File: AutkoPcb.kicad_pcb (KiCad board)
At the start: 2 copper layers, 83.8 x 105.5 mm, 60 parts, among them IC201 TEENSY_4.1, J101 JST 2.56mm, J102 JST 2.56mm, J103 JST 2.56mm, J104 JST 2.56mm, J105 JST 2.56mm, J107 JST 2.56mm, J108 JST 2.56mm, J109 JST 2.56mm, J110 JST 2.56mm, J111 JST 2.56mm, J112 JST 2.56mm, J113 JST 2.56mm, J114 Conn_01x12_Pin, J401 Conn_01x03_Male, J501 Conn_01x03_Male, J601 JST 2.56mm, J701 JST 2.56mm, J801 JST 2.56mm, J901 ARK 5mm, J902 Barrel_Jack_MountingPin, J903 Barrel_Jack_MountingPin, J904 ARK 5mm, J905 JST 2.54mm, J906 JST 2.54mm, J907 JST 2.56mm, SW1001 SW_Push, SW1101 SW_Push, SW1201 SW_Push, SW1301 SW_Push, U901 AZ1117-3.3

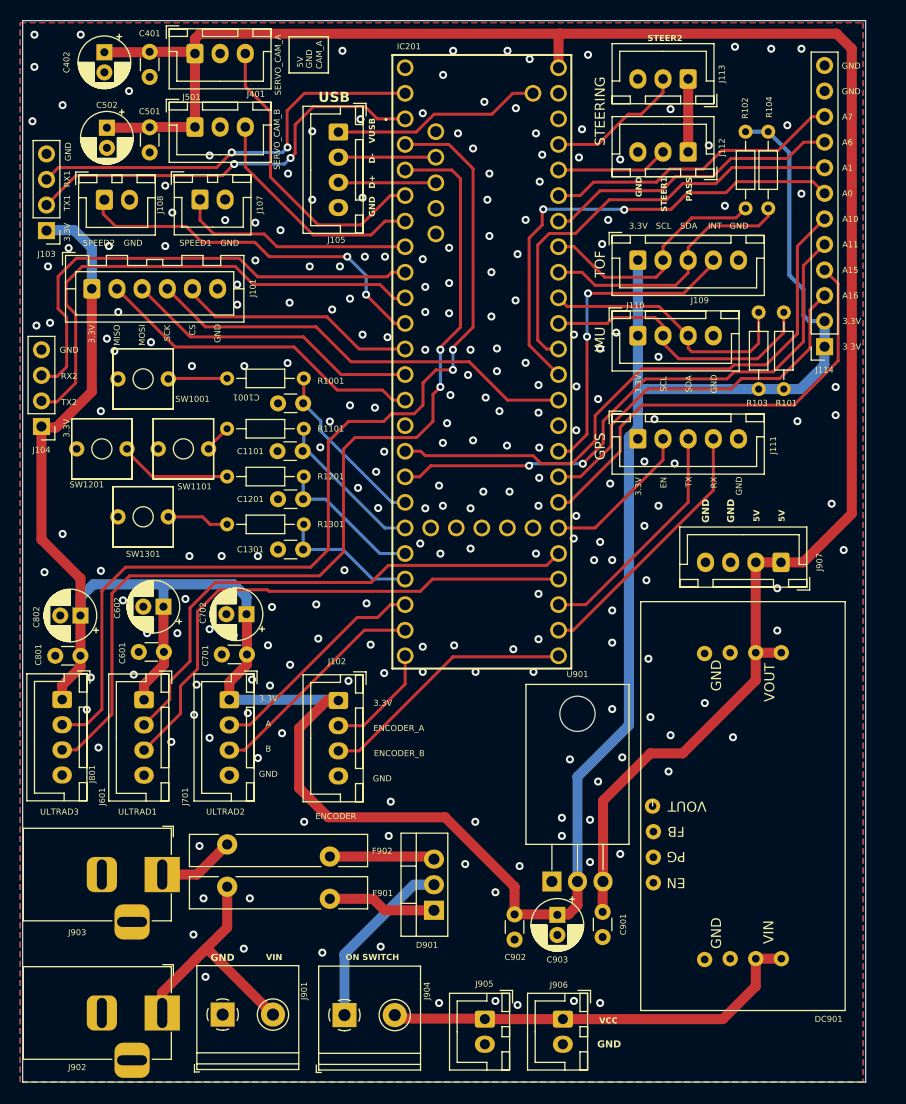
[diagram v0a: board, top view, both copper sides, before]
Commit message: changing labels on PCB
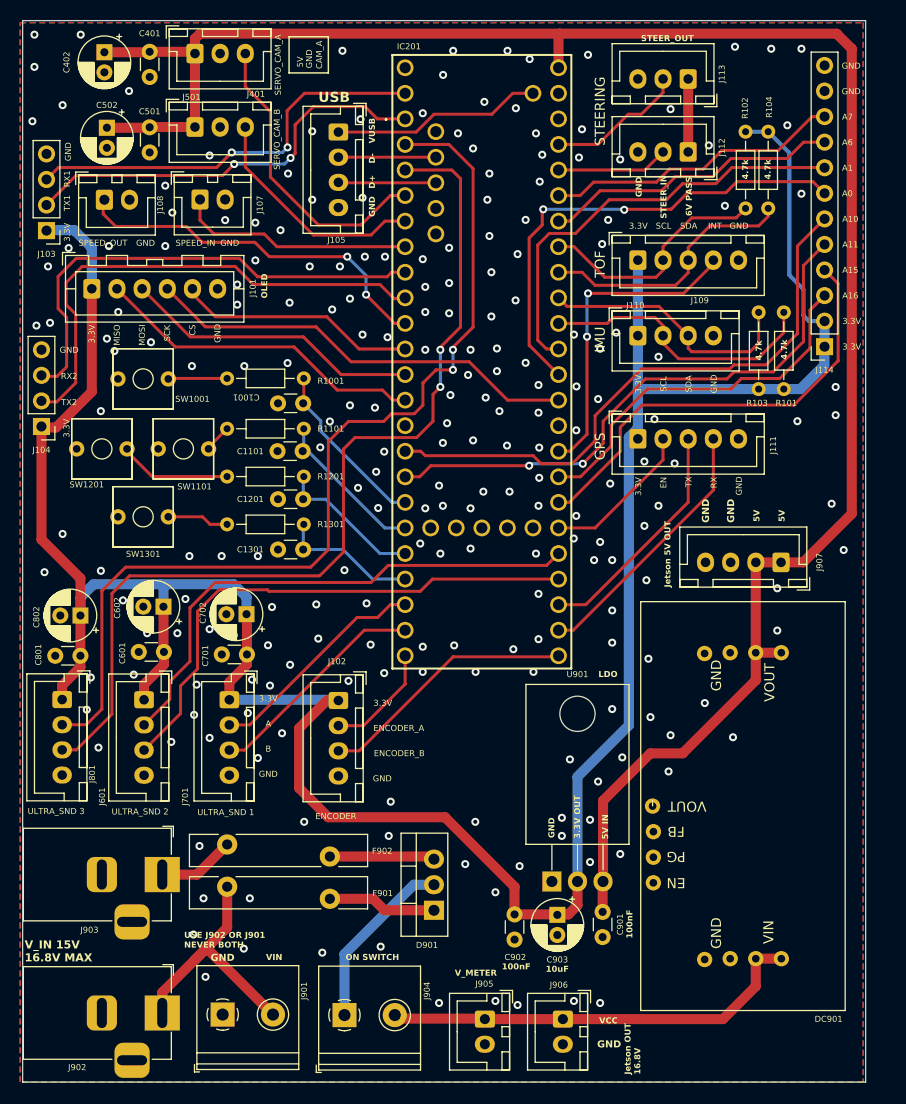
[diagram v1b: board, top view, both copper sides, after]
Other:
- board text added: "100nF"
- board text added: "10uF"
- board text added: "3.3V OUT"
- board text added: "4.7k"
- board text added: "5V IN"
- board text added: "6V PASS"
- board text added: "Jetson 5V OUT"
- board text added: "Jetson OUT 16.8V"
- board text added: "LDO"
- board text added: "OLED"
- board text added: "SPEED_IN"
- board text added: "SPEED_OUT"
- board text added: "STEER_IN"
- board text added: "STEER_OUT"
- board text added: "ULTRA_SND 1"
- board text added: "ULTRA_SND 2"
- board text added: "ULTRA_SND 3"
- board text added: "USE J902 OR J901 NEVER BOTH"
- board text added: "V_IN 15V 16.8V MAX"
- board text added: "V_METER"
- board text removed: "PASS"
- board text removed: "SPEED1"
- board text removed: "SPEED2"
- board text removed: "STEER1"
- board text removed: "STEER2"
- board text removed: "ULTRAD1"
- board text removed: "ULTRAD2"
- board text removed: "ULTRAD3"
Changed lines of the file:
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@@
     (property "ki_keywords" "cap capacitor")
     (attr through_hole)
-    (fp_text reference "C901" (at 1.25 -2.05 90 unlocked) (layer "F.SilkS")
+    (fp_text reference "C901" (at 1.244212 -1.743767 90 unlocked) (layer "F.SilkS")
         (effects (font (size 0.6 0.6) (thickness 0.15)))
     )
@@
     (property "ki_keywords" "DC power barrel jack connector")
     (attr through_hole)
-    (fp_text reference "J903" (at -8.45 5.75 unlocked) (layer "F.SilkS")
+    (fp_text reference "J903" (at -7.234083 5.500901 unlocked) (layer "F.SilkS")
         (effects (font (size 0.6 0.6) (thickness 0.15)))
     )
@@
   (gr_rect (start 104.63 24.205) (end 188.38 129.655)
     (stroke (width 0.1) (type solid)) (fill none) (layer "Edge.Cuts"))
+  (gr_text "10uF" (at 156.603213 118.774295) (layer "F.SilkS")
+    (effects (font (size 0.6 0.6) (thickness 0.15) bold) (justify left bottom))
+  )
   (gr_text "TOF" (at 162 48.4 90) (layer "F.SilkS")
     (effects (font (size 1 1) (thickness 0.15)))
@@
     (effects (font (size 0.6 0.6) (thickness 0.15)))
   )
-  (gr_text "STEER2" (at 166.7 26.3) (layer "F.SilkS")
+  (gr_text "STEER_OUT" (at 166.056761 26.313582) (layer "F.SilkS")
+    (effects (font (size 0.6 0.6) (thickness 0.15) bold) (justify left bottom))
+  )
+  (gr_text "USE J902 OR J901\nNEVER BOTH" (at 120.668249 116.371353) (layer "F.SilkS")
+    (effects (font (size 0.6 0.6) (thickness 0.15) bold) (justify left bottom))
+  )
+  (gr_text "OLED" (at 129.001903 51.799877 90) (layer "F.SilkS")
     (effects (font (size 0.6 0.6) (thickness 0.15) bold) (justify left bottom))
   )
@@
     (effects (font (size 0.6 0.6) (thickness 0.15)))
   )
+  (gr_text "GND" (at 157.526256 105.414432 90) (layer "F.SilkS")
+    (effects (font (size 0.6 0.6) (thickness 0.15) bold) (justify left bottom))
+  )
   (gr_text "GND" (at 186.942856 28.7) (layer "F.SilkS")
     (effects (font (size 0.6 0.6) (thickness 0.15)))
@@
     (effects (font (size 0.6 0.6) (thickness 0.15) bold) (justify left bottom))
   )
+  (gr_text "V_IN 15V\n16.8V MAX\n" (at 104.829506 117.765246) (layer "F.SilkS")
+    (effects (font (size 0.8 0.8) (thickness 0.15) bold) (justify left bottom))
+  )
   (gr_text "RX" (at 173.3 70.1 90) (layer "F.SilkS")
     (effects (font (size 0.6 0.6) (thickness 0.15)))
@@
     (effects (font (size 0.6 0.6) (thickness 0.15) bold) (justify left bottom))
   )
-  (gr_text "ULTRAD3" (at 108.285 102.805) (layer "F.SilkS")
+  (gr_text "ULTRA_SND 3" (at 107.954328 102.751444) (layer "F.SilkS")
     (effects (font (size 0.6 0.6) (thickness 0.15)))
   )
@@
     (effects (font (size 0.6 0.6) (thickness 0.15)))
   )
-  (gr_text "ULTRAD1" (at 116.035 102.805) (layer "F.SilkS")
+  (gr_text "ULTRA_SND 2" (at 116.296866 102.794894) (layer "F.SilkS")
     (effects (font (size 0.6 0.6) (thickness 0.15)))
   )
+  (gr_text "4.7k" (at 179.013684 39.988927 90) (layer "F.SilkS")
+    (effects (font (size 0.6 0.6) (thickness 0.15) bold) (justify left bottom))
+  )
   (gr_text "SERVO_CAM_B" (at 129.9 36 90) (layer "F.SilkS")
     (effects (font (size 0.6 0.6) (thickness 0.15)))
@@
     (effects (font (size 0.6 0.6) (thickness 0.15)))
   )
-  (gr_text "SPEED2" (at 112.2 46.3) (layer "F.SilkS")
+  (gr_text "SPEED_OUT" (at 112.61277 46.290289) (layer "F.SilkS")
     (effects (font (size 0.6 0.6) (thickness 0.15)))
   )
@@
     (effects (font (size 1 1) (thickness 0.15)))
   )
-  (gr_text "STEER1" (at 168.7 43.2 90) (layer "F.SilkS")
+  (gr_text "STEER_IN\n" (at 168.662426 43.879478 90) (layer "F.SilkS")
     (effects (font (size 0.6 0.6) (thickness 0.15) bold) (justify left bottom))
   )
-  (gr_text "ULTRAD2" (at 124.785 102.805) (layer "F.SilkS")
+  (gr_text "ULTRA_SND 1" (at 124.813206 102.86007) (layer "F.SilkS")
     (effects (font (size 0.6 0.6) (thickness 0.15)))
   )
@@
     (effects (font (size 0.6 0.6) (thickness 0.15)))
   )
-  (gr_text "SPEED1" (at 121.8 46.3) (layer "F.SilkS")
+  (gr_text "SPEED_IN" (at 121.8 46.3) (layer "F.SilkS")
     (effects (font (size 0.6 0.6) (thickness 0.15)))
   )
@@
     (effects (font (size 0.6 0.6) (thickness 0.15)))
   )
-  (gr_text "PASS" (at 171.2 42.171429 90) (layer "F.SilkS")
+  (gr_text "V_METER" (at 147.559548 119.163502) (layer "F.SilkS")
+    (effects (font (size 0.6 0.6) (thickness 0.15) bold) (justify left bottom))
+  )
+  (gr_text "6V PASS" (at 171.183984 43.619567 90) (layer "F.SilkS")
     (effects (font (size 0.6 0.6) (thickness 0.15) bold) (justify left bottom))
   )
@@
     (effects (font (size 0.6 0.6) (thickness 0.15) bold) (justify left bottom))
   )
-  (gr_text "GND" (at 115.6 46.3) (layer "F.SilkS")
+  (gr_text "3.3V OUT" (at 160.088889 105.475447 90) (layer "F.SilkS")
+    (effects (font (size 0.6 0.6) (thickness 0.15) bold) (justify left bottom))
+  )
+  (gr_text "GND" (at 116.84 46.3) (layer "F.SilkS")
     (effects (font (size 0.6 0.6) (thickness 0.15)))
   )
+  (gr_text "4.7k" (at 180.644755 57.88915 90) (layer "F.SilkS")
+    (effects (font (size 0.6 0.6) (thickness 0.15) bold) (justify left bottom))
+  )
   (gr_text "GND" (at 172.9 74.1 90) (layer "F.SilkS")
     (effects (font (size 0.7 0.7) (thickness 0.15) bold) (justify left bottom))
@@
     (effects (font (size 0.7 0.7) (thickness 0.15) bold) (justify left bottom))
   )
+  (gr_text "Jetson OUT\n16.8V" (at 166.063102 128.910918 90) (layer "F.SilkS")
+    (effects (font (size 0.6 0.6) (thickness 0.15) bold) (justify left bottom))
+  )
   (gr_text "A" (at 129.035 94.055) (layer "F.SilkS")
     (effects (font (size 0.6 0.6) (thickness 0.15)))
@@
     (effects (font (size 0.6 0.6) (thickness 0.15)))
   )
+  (gr_text "4.7k" (at 178.119912 57.971482 90) (layer "F.SilkS")
+    (effects (font (size 0.6 0.6) (thickness 0.15) bold) (justify left bottom))
+  )
   (gr_text "GND" (at 129.035 99.055) (layer "F.SilkS")
     (effects (font (size 0.6 0.6) (thickness 0.15)))
@@
     (effects (font (size 0.6 0.6) (thickness 0.15)))
   )
+  (gr_text "Jetson 5V OUT" (at 169.055051 80.517625 90) (layer "F.SilkS")
+    (effects (font (size 0.6 0.6) (thickness 0.15) bold) (justify left bottom))
+  )
   (gr_text "GND" (at 186.942856 31.236363) (layer "F.SilkS")
     (effects (font (size 0.6 0.6) (thickness 0.15)))
   )
+  (gr_text "4.7k" (at 176.783891 39.988927 90) (layer "F.SilkS")
+    (effects (font (size 0.6 0.6) (thickness 0.15) bold) (justify left bottom))
+  )
   (gr_text "A16" (at 186.857143 51.527267) (layer "F.SilkS")
     (effects (font (size 0.6 0.6) (thickness 0.15)))
@@
     (effects (font (size 0.6 0.6) (thickness 0.15)))
   )
+  (gr_text "5V IN" (at 162.865075 105.536462 90) (layer "F.SilkS")
+    (effects (font (size 0.6 0.6) (thickness 0.15) bold) (justify left bottom))
+  )
   (gr_text "ENCODER_A\n" (at 142 94.5) (layer "F.SilkS")
     (effects (font (size 0.6 0.6) (thickness 0.15)))
@@
     (effects (font (size 1 1) (thickness 0.15) bold) (justify left bottom))
   )
+  (gr_text "LDO" (at 161.827819 89.489497) (layer "F.SilkS")
+    (effects (font (size 0.6 0.6) (thickness 0.15) bold) (justify left bottom))
+  )
+  (gr_text "100nF" (at 152.229307 118.532356) (layer "F.SilkS")
+    (effects (font (size 0.6 0.6) (thickness 0.15) bold) (justify left bottom))
+  )
   (gr_text "TX1" (at 109.05 42.325 90) (layer "F.SilkS")
     (effects (font (size 0.6 0.6) (thickness 0.15)))
@@
     (effects (font (size 0.6 0.6) (thickness 0.15)))
   )
+  (gr_text "100nF" (at 165.279875 115.397239 90) (layer "F.SilkS")
+    (effects (font (size 0.6 0.6) (thickness 0.15) bold) (justify left bottom))
+  )
   (dimension (type aligned) (layer "Dwgs.User")

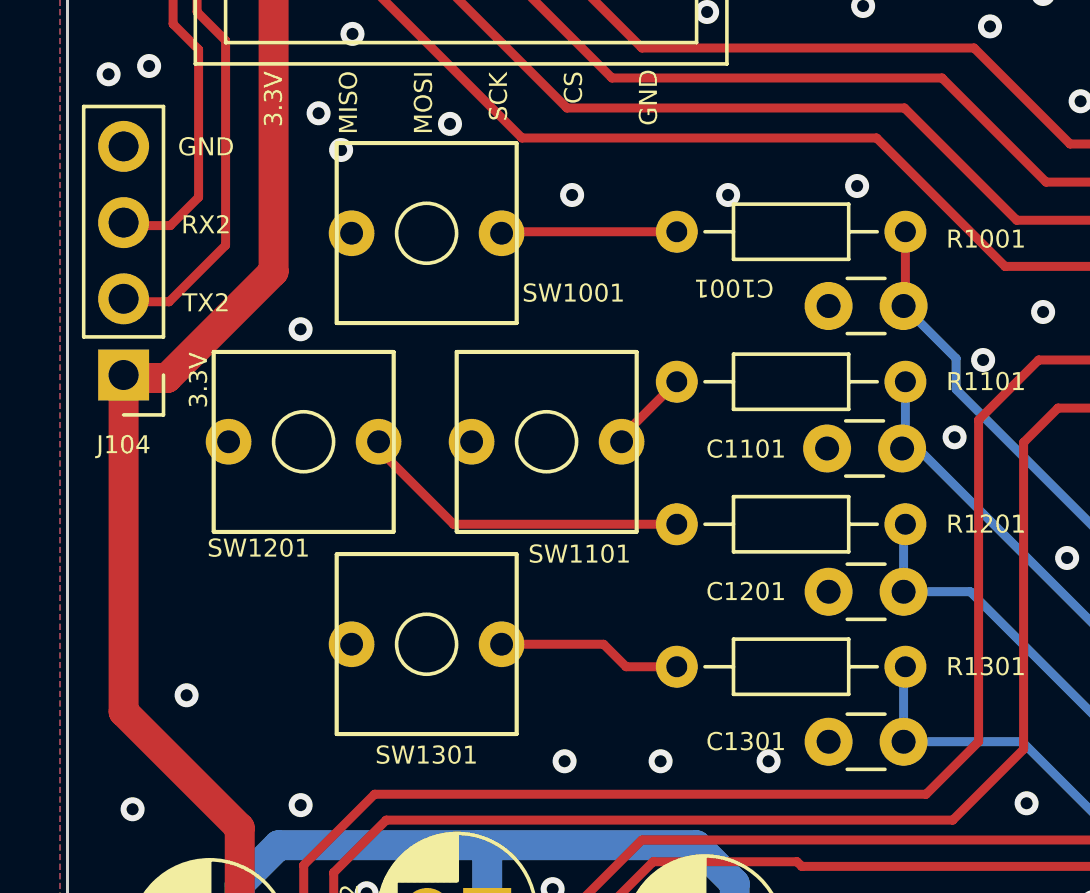
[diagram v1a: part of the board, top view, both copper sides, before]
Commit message: [FEAT] Zaktualizowano układ do debauncing
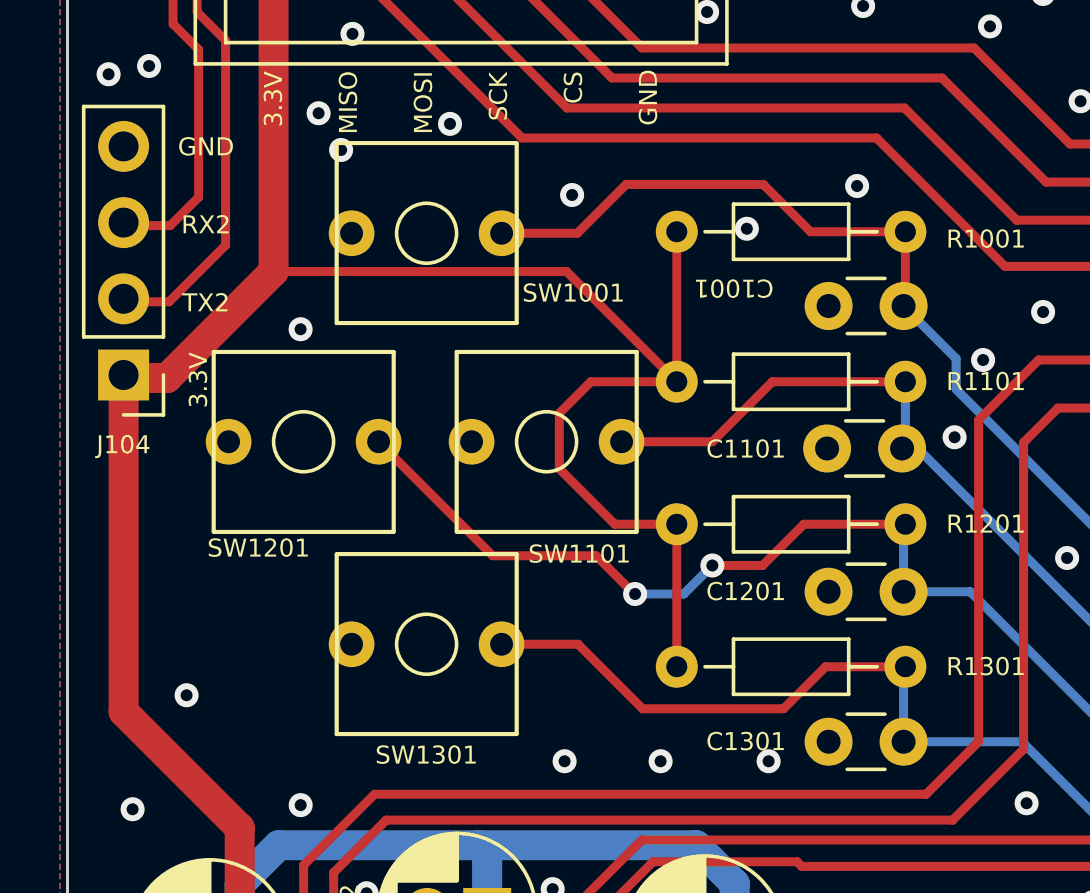
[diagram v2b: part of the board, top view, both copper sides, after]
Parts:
- R1001, R1101, R1201, R1301: value 100R -> 10k
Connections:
- net /SPEED1 renamed /SPEED_IN
- net /SPEED2 renamed /SPEED_OUT
- net /STEERING1 renamed /STEERING_IN
- net /STEERING2 renamed /STEERING_OUT
- R1001 pad 2: Net-(R1001-Pad2) -> +3.3V
- R1101 pad 2: Net-(R1101-Pad2) -> +3.3V
- R1201 pad 2: Net-(R1201-Pad2) -> +3.3V
- R1301 pad 2: Net-(R1301-Pad2) -> +3.3V
- SW1001 pad 1: Net-(R1001-Pad2) -> /BUTTON_A
- SW1101 pad 1: Net-(R1101-Pad2) -> /BUTTON_B
- SW1201 pad 1: Net-(R1201-Pad2) -> /BUTTON_C
- SW1301 pad 1: Net-(R1301-Pad2) -> /BUTTON_D
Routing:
- net +3.3V: track 269.7 -> 311.8 mm
- net /BUTTON_C: track 14.6 -> 35.2 mm, vias 0 -> 2
- net /BUTTON_D: track 13.8 -> 29.1 mm
- net /BUTTON_A: track 17.2 -> 32.0 mm
- net Net-(R1201-Pad2): track 11.3 -> 0.00 mm
- net /BUTTON_B: track 14.9 -> 25.2 mm
- net Net-(R1301-Pad2): track 6.55 -> 0.00 mm
- net Net-(R1001-Pad2): track 5.69 -> 0.00 mm
- net Net-(R1101-Pad2): track 2.83 -> 0.00 mm
